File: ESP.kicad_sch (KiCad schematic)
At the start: 4 parts, among them SW1 RESET, U1 ESP32-C6-MINI-1/U

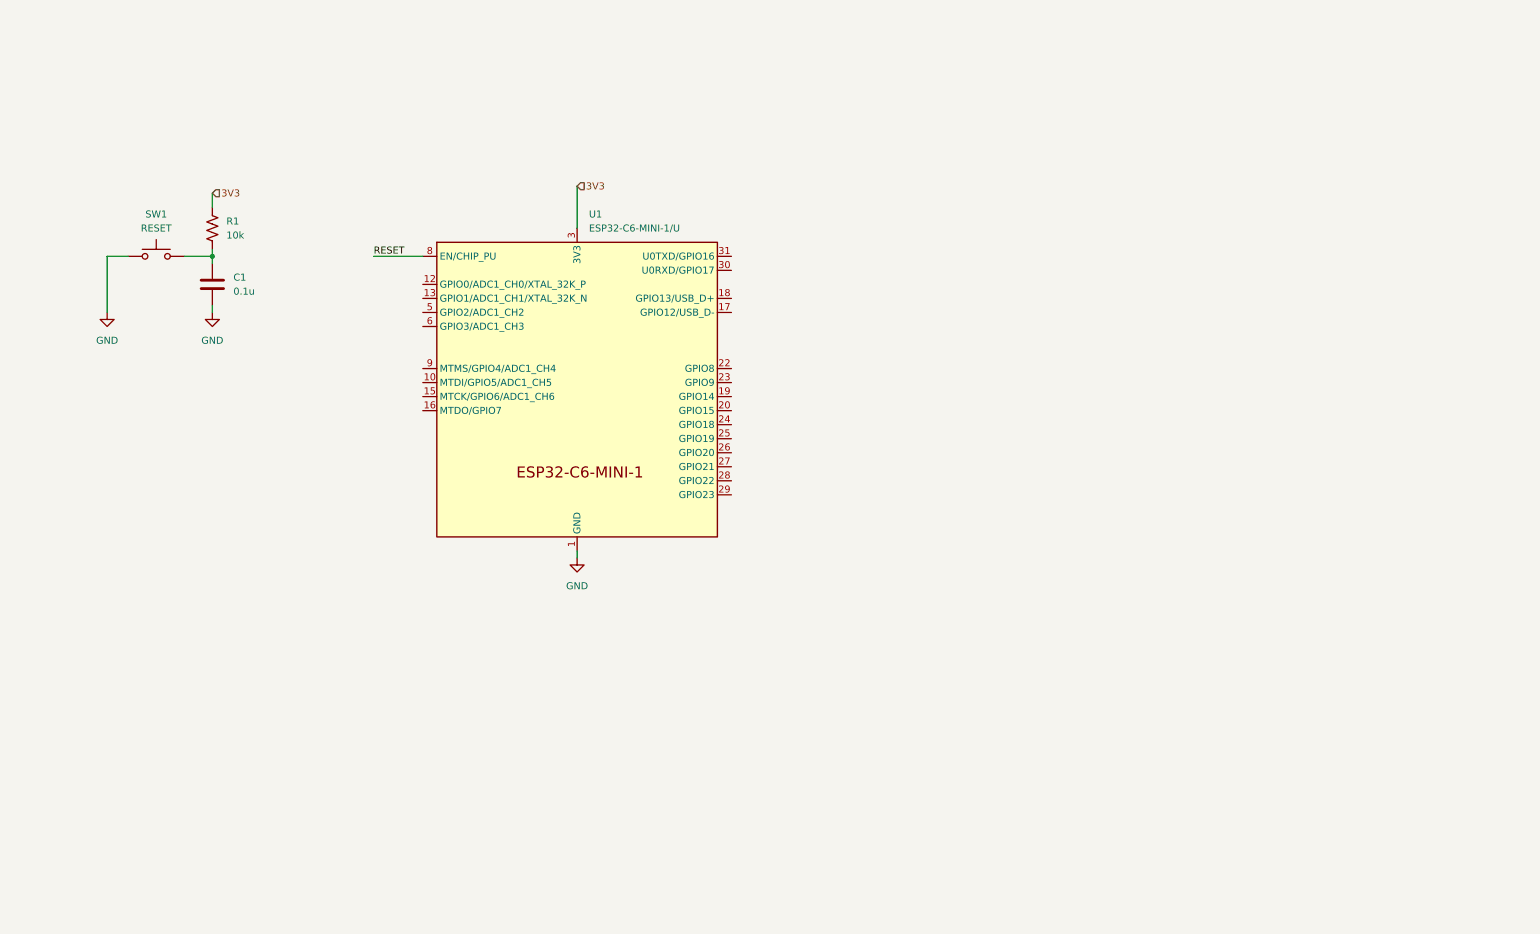
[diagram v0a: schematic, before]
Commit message: sch for review missing LSOM
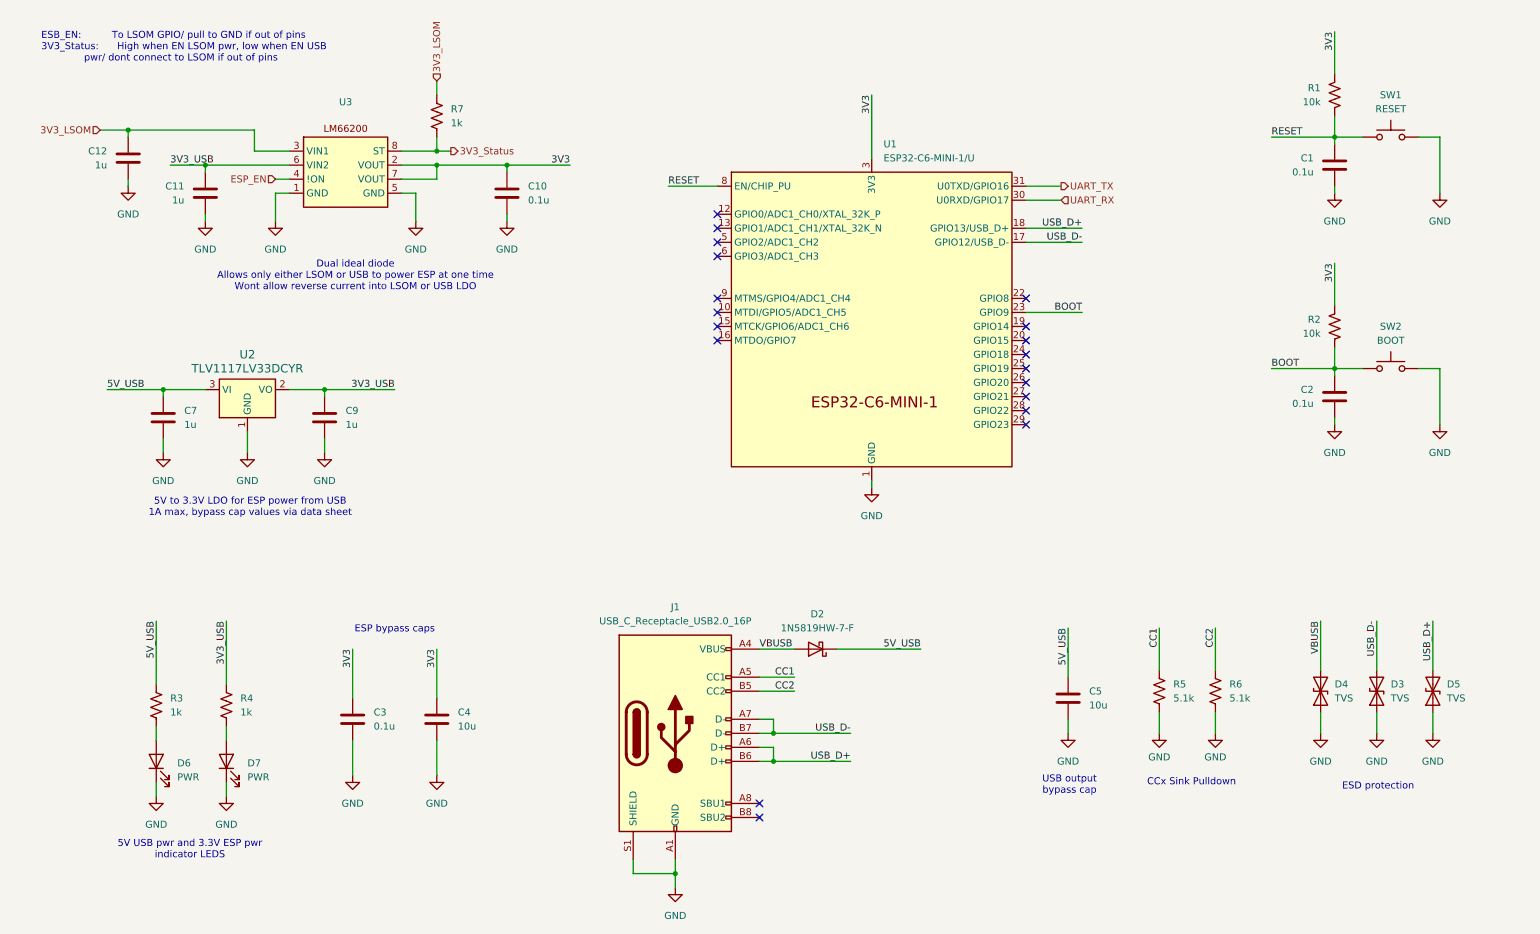
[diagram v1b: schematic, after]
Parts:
- added C10: 0.1u, Capacitor_SMD:C_0603_1608Metric, symbol Device:C
- added C11, C12, C7, C9: 1u, Capacitor_SMD:C_0603_1608Metric, symbol Device:C
- added C2, C3: 0.1u, symbol Device:C
- added C4: 10u, symbol Device:C
- added C5: 10u, Capacitor_SMD:C_0603_1608Metric, symbol Device:C
- added D2: 1N5819HW-7-F, Diode_SMD:D_SOD-123, symbol Device:D_Schottky
- added D3, D4, D5: TVS, Diode_SMD:D_0603_1608Metric, symbol Device:D_TVS
- added D6, D7: PWR, LED_SMD:LED_0603_1608Metric, symbol Device:LED
- added J1: USB_C_Receptacle_USB2.0_16P, Connector_USB:USB_C_Receptacle_GCT_USB4105-xx-A_16P_TopMnt_Horizontal, symbol Connector:USB_C_Receptacle_USB2.0_16P
- added R2: 10k, symbol Device:R_US
- added R3, R4, R7: 1k, symbol Device:R_US
- added R5, R6: 5.1k, symbol Device:R_US
- added SW2: BOOT, symbol Switch:SW_MEC_5G
- added U2: TLV1117LV33DCYR, Package_TO_SOT_SMD:SOT-223-3_TabPin2, symbol Regulator_Linear:AMS1117-3.3
- added U3: ~, symbol VCU:LM66200
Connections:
- net 3V3: now also C10.1, C3.1, C4.1, R2.1, U3.2 (VOUT), U3.7 (VOUT)
- net GND: now also C10.2, C11.2, C12.2, C2.2, C3.2, C4.2, C5.2, C7.2, C9.2, D3.1 (A1), D4.1 (A1), D5.1 (A1), D6.1 (K), D7.1 (K), J1.A1 (GND), J1.A12 (GND), J1.B1 (GND), J1.B12 (GND), J1.S1 (SHIELD), R5.2, R6.2, SW2.1 (A), SW2.2 (A), U2.1 (GND), U3.1 (GND), U3.5 (GND)
- net RESET: now also C1.1, R1.2, SW1.3 (B), SW1.4 (B)
- net USB_D-: now reaches U1.17 (GPIO12/USB_D-)
- net USB_D-: now also D3.2 (A2), J1.A7 (D-), J1.B7 (D-)
- net USB_D+: now reaches U1.18 (GPIO13/USB_D+)
- net USB_D+: now also D5.2 (A2), J1.A6 (D+), J1.B6 (D+)
- net BOOT: now reaches U1.23 (GPIO9)
- net BOOT: now also C2.1, R2.2, SW2.3 (B), SW2.4 (B)
- net UART_RX: now reaches U1.30 (U0RXD/GPIO17)
- net UART_TX: now reaches U1.31 (U0TXD/GPIO16)
- new net: D6.2 (A), R3.2
- new net: D7.2 (A), R4.2
- new net 3V3_LSOM: C12.1, R7.1, U3.3 (VIN1)
- new net 3V3_Status: R7.2, U3.8 (ST)
- new net 3V3_USB: C11.1, C9.1, R4.1, U2.2 (VO), U3.6 (VIN2)
- new net 5V_USB: C5.1, C7.1, D2.1 (K), R3.1, U2.3 (VI)
- new net CC1: J1.A5 (CC1), R5.1
- new net CC2: J1.B5 (CC2), R6.1
- new net ESP_EN: U3.4 (!ON)
- new net VBUSB: D2.2 (A), D4.2 (A2), J1.A4 (VBUS), J1.A9 (VBUS), J1.B4 (VBUS), J1.B9 (VBUS)
- no-connect marks 0 -> 19
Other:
- note added: "5V USB pwr and 3.3V ESP pwr indicator LEDS"
- note added: "5V to 3.3V LDO for ESP power from USB 1A max, bypass cap values via data sheet"
- note added: "CCx Sink Pulldown"
- note added: "Dual ideal diode Allows only either LSOM or USB to power ESP at one time Wont allow reverse current into LSOM or USB LDO"
- note added: "ESB_EN: To LSOM GPIO/ pull to GND if out of pins 3V3_Status: High when EN LSOM pwr, low when EN USB pwr/ dont connect to LSOM if out of pins"
- note added: "ESD protection"
- note added: "ESP bypass caps"
- note added: "USB output bypass cap"
- moved on the sheet: C1, R1, SW1, U1

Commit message: review LSOM
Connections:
- net 3V3_Status: no longer names the net of R7.2, U3.8 (ST)
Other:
- note added: "3V3_Status"
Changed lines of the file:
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@@
+		)
+	)
+	(text "3V3_Status"
+		(exclude_from_sim no)
+		(at 95.504 40.132 0)
+		(effects
+			(font
+				(size 1.27 1.27)
+			)
 		)
 	)
@@
 	)
 	(junction
-		(at 90.17 40.64)
-		(diameter 0)
-		(color 0 0 0 0)
-	)
-	(junction
 		(at 252.73 38.1)
 		(diameter 0)
@@
 	(wire
 		(pts
-			(xy 90.17 40.64) (xy 92.71 40.64)
-		)
-		(stroke
-			(width 0)
-			(type default)
-		)
-	)
-	(wire
-		(pts
 			(xy 148.59 151.13) (xy 151.13 151.13)
 		)
@@
 		)
 	)
-	(hierarchical_label "3V3_Status"
-		(shape output)
-		(at 92.71 40.64 0)
-		(effects
-			(font
-				(size 1.27 1.27)
-			)
-			(justify left)
-		)
-	)

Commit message: review sch one last time
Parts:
- removed C1, C2: 0.1u, symbol Device:C
- removed R1, R2: 10k, symbol Device:R_US
- removed SW1: RESET, symbol Switch:SW_MEC_5G
- removed SW2: BOOT, symbol Switch:SW_MEC_5G
- added J14: UART_Breakout, symbol Connector_Generic:Conn_01x02
- added R8: 10k, symbol Device:R_US
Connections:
- net GND: now also R8.2
- net UART_RX: now also J14.2 (Pin_2)
- net UART_TX: now also J14.1 (Pin_1)
- net LED1: now reaches U1.19 (GPIO14)
- net LED2: now reaches U1.20 (GPIO15)
- net LED3: now reaches U1.24 (GPIO18)
- net LED4: now reaches U1.25 (GPIO19)
- net IO1: now reaches U1.26 (GPIO20)
- net IO2: now reaches U1.27 (GPIO21)
- net IO3: now reaches U1.28 (GPIO22)
- net IO4: now reaches U1.29 (GPIO23)
- net ESP_EN: no longer names the net of U3.4 (!ON)
- net ESP_EN: now also R8.1
- no-connect marks 19 -> 11
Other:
- added sheet Buttons_LEDs_IO (Buttond_LEDs_IO.kicad_sch)
- note removed: "3V3_Status"
- note removed: "ESB_EN: To LSOM GPIO/ pull to GND if out of pins 3V3_Status: High when EN LSOM pwr, low when EN USB pwr/ dont connect to LSOM if out of pins"
- moved on the sheet: C10, C11, C12, C3, C4, C5, D2, D3, D4, D5, D6, D7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

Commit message: added opto's to sense signals
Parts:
- C3, C4: footprint (none) -> Capacitor_SMD:C_0805_2012Metric
- R3, R4, R5, R6, R7, R8: footprint (none) -> Resistor_SMD:R_0805_2012Metric
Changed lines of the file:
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@@
 			)
 		)
-		(property "Footprint" ""
+		(property "Footprint" "Resistor_SMD:R_0805_2012Metric"
 			(at 58.166 51.054 90)
 			(effects
@@
 			)
 		)
-		(property "Footprint" ""
+		(property "Footprint" "Capacitor_SMD:C_0805_2012Metric"
 			(at 55.5752 151.13 0)
 			(effects
@@
 			)
 		)
-		(property "Footprint" ""
+		(property "Footprint" "Resistor_SMD:R_0805_2012Metric"
 			(at 25.146 141.224 90)
 			(effects
@@
 			)
 		)
-		(property "Footprint" ""
+		(property "Footprint" "Resistor_SMD:R_0805_2012Metric"
 			(at 37.846 141.224 90)
 			(effects
@@
 			)
 		)
-		(property "Footprint" ""
+		(property "Footprint" "Resistor_SMD:R_0805_2012Metric"
 			(at 94.996 34.544 90)
 			(effects
@@
 			)
 		)
-		(property "Footprint" ""
+		(property "Footprint" "Resistor_SMD:R_0805_2012Metric"
 			(at 215.646 139.954 90)
 			(effects
@@
 			)
 		)
-		(property "Footprint" ""
+		(property "Footprint" "Capacitor_SMD:C_0805_2012Metric"
 			(at 68.8848 151.13 0)
 			(effects
@@
 			)
 		)
-		(property "Footprint" ""
+		(property "Footprint" "Resistor_SMD:R_0805_2012Metric"
 			(at 225.806 139.954 90)
 			(effects

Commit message: layout start
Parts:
- J13: renamed from J14; footprint (none) -> Connector_PinHeader_2.54mm:PinHeader_1x02_P2.54mm_Vertical
- U2: renamed from U3; footprint (none) -> LM66200:SOTFL50P160X60-8N
- U3: renamed from U1; footprint PCM_Espressif:ESP32-C6-MINI-1 -> ESP32-C6-MINI-1:ESP32-C6-MINI-1
- renumbered C5 to C10, C12 to C3, C7 to C4, C11 to C5, C3 to C6, C9 to C7, C4 to C8, C10 to C9, D6 to D2, D7 to D3, D2 to D4, D4 to D5, D3 to D6, D5 to D7, J1 to J12, R4 to R10, R8 to R11, R7 to R12, R5 to R13, R6 to R14, R3 to R9, U2 to U1

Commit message: first revision
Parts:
- J12: footprint Connector_USB:USB_C_Receptacle_GCT_USB4105-xx-A_16P_TopMnt_Horizontal -> USBC:GCT_USB4215-03-A_REVA
- renumbered C10 to C11, D5 to D6, D6 to D7, D7 to D8
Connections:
- net GND: now also J12.S2 (SHIELD), J12.S3 (SHIELD), J12.S4 (SHIELD)
- net IO12: now reaches U3.10 (MTDI/GPIO5/ADC1_CH5)
- net IO5: now reaches U3.12 (GPIO0/ADC1_CH0/XTAL_32K_P)
- net IO6: now reaches U3.13 (GPIO1/ADC1_CH1/XTAL_32K_N)
- net IO7: now reaches U3.15 (MTCK/GPIO6/ADC1_CH6)
- net IO8: now reaches U3.16 (MTDO/GPIO7)
- net IO9: now reaches U3.5 (GPIO2/ADC1_CH2)
- net IO10: now reaches U3.6 (GPIO3/ADC1_CH3)
- net IO11: now reaches U3.9 (MTMS/GPIO4/ADC1_CH4)
- no-connect marks 11 -> 3
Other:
- sheet Buttons_LEDs_IO ports: added IO10, IO11, IO12, IO5, IO6, IO7, IO8, IO9; removed none

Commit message: fixed
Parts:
- renumbered C11 to C10, D6 to D5, D7 to D6, D8 to D7
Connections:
- net IO1: now also U3.29 (GPIO23); no longer U3.26 (GPIO20)
- net IO10: now also U3.9 (MTMS/GPIO4/ADC1_CH4); no longer U3.6 (GPIO3/ADC1_CH3)
- net IO11: now also U3.6 (GPIO3/ADC1_CH3); no longer U3.9 (MTMS/GPIO4/ADC1_CH4)
- net IO12: now also U3.5 (GPIO2/ADC1_CH2); no longer U3.10 (MTDI/GPIO5/ADC1_CH5)
- net IO2: now also U3.28 (GPIO22); no longer U3.27 (GPIO21)
- net IO3: now also U3.27 (GPIO21); no longer U3.28 (GPIO22)
- net IO4: now also U3.26 (GPIO20); no longer U3.29 (GPIO23)
- net IO5: now also U3.16 (MTDO/GPIO7); no longer U3.12 (GPIO0/ADC1_CH0/XTAL_32K_P)
- net IO6: now also U3.15 (MTCK/GPIO6/ADC1_CH6); no longer U3.13 (GPIO1/ADC1_CH1/XTAL_32K_N)
- net IO7: now also U3.13 (GPIO1/ADC1_CH1/XTAL_32K_N); no longer U3.15 (MTCK/GPIO6/ADC1_CH6)
- net IO8: now also U3.12 (GPIO0/ADC1_CH0/XTAL_32K_P); no longer U3.16 (MTDO/GPIO7)
- net IO9: now also U3.10 (MTDI/GPIO5/ADC1_CH5); no longer U3.5 (GPIO2/ADC1_CH2)
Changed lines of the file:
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@@
 		)
 	)
-	(label "IO12"
+	(label "IO9"
 		(at 137.16 66.04 0)
 		(effects
@@
 		)
 	)
-	(label "IO7"
+	(label "IO6"
 		(at 137.16 68.58 0)
 		(effects
@@
 		)
 	)
-	(label "IO1"
+	(label "IO4"
 		(at 213.36 78.74 180)
 		(effects
@@
 		)
 	)
-	(label "IO9"
+	(label "IO12"
 		(at 137.16 53.34 0)
 		(effects
@@
 		)
 	)
-	(label "IO11"
+	(label "IO10"
 		(at 137.16 63.5 0)
 		(effects
@@
 		)
 	)
-	(label "IO3"
+	(label "IO2"
 		(at 213.36 83.82 180)
 		(effects
@@
 		)
 	)
-	(label "IO6"
+	(label "IO7"
 		(at 137.16 50.8 0)
 		(effects
@@
 		)
 	)
-	(label "IO5"
+	(label "IO8"
 		(at 137.16 48.26 0)
 		(effects
@@
 		)
 	)
-	(label "IO4"
+	(label "IO1"
 		(at 213.36 86.36 180)
 		(effects
@@
 		)
 	)
-	(label "IO8"
+	(label "IO5"
 		(at 137.16 71.12 0)
 		(effects
@@
 		)
 	)
-	(label "IO10"
+	(label "IO11"
 		(at 137.16 55.88 0)
 		(effects
@@
 		)
 	)
-	(label "IO2"
+	(label "IO3"
 		(at 213.36 81.28 180)
 		(effects
@@
 		(on_board yes)
 		(dnp no)
-		(property "Reference" "#PWR036"
+		(property "Reference" "#PWR034"
 			(at 214.63 153.67 0)
 			(effects
@@
 			(project "VehicleControlUnit"
 				(path "/795c8e51-3ded-4d21-b864-aaff31c5def7/6282503b-e4ab-454b-a074-f701a067f39b"
-					(reference "#PWR036")
+					(reference "#PWR034")
 					(unit 1)
 				)
@@
 		(dnp no)
 		(fields_autoplaced yes)
-		(property "Reference" "#PWR034"
+		(property "Reference" "#PWR032"
 			(at 175.26 104.14 0)
 			(effects
@@
 			(project ""
 				(path "/795c8e51-3ded-4d21-b864-aaff31c5def7/6282503b-e4ab-454b-a074-f701a067f39b"
-					(reference "#PWR034")
+					(reference "#PWR032")
 					(unit 1)
 				)
@@
 		(dnp no)
 		(fields_autoplaced yes)
-		(property "Reference" "D7"
+		(property "Reference" "D6"
 			(at 256.54 138.4299 90)
 			(effects
@@
 			(project "VehicleControlUnit"
 				(path "/795c8e51-3ded-4d21-b864-aaff31c5def7/6282503b-e4ab-454b-a074-f701a067f39b"
-					(reference "D7")
+					(reference "D6")
 					(unit 1)
 				)
@@
 		(dnp no)
 		(fields_autoplaced yes)
-		(property "Reference" "#PWR035"
+		(property "Reference" "#PWR033"
 			(at 198.12 153.67 0)
 			(effects
@@
 			(project "VehicleControlUnit"
 				(path "/795c8e51-3ded-4d21-b864-aaff31c5def7/6282503b-e4ab-454b-a074-f701a067f39b"
-					(reference "#PWR035")
+					(reference "#PWR033")
 					(unit 1)
 				)
@@
 		(dnp no)
 		(fields_autoplaced yes)
-		(property "Reference" "#PWR039"
+		(property "Reference" "#PWR037"
 			(at 254 153.67 0)
 			(effects
@@
 			(project "VehicleControlUnit"
 				(path "/795c8e51-3ded-4d21-b864-aaff31c5def7/6282503b-e4ab-454b-a074-f701a067f39b"
-					(reference "#PWR039")
+					(reference "#PWR037")
 					(unit 1)
 				)
@@
 		(dnp no)
 		(fields_autoplaced yes)
-		(property "Reference" "#PWR038"
+		(property "Reference" "#PWR036"
 			(at 243.84 153.67 0)
 			(effects
@@
 			(project "VehicleControlUnit"
 				(path "/795c8e51-3ded-4d21-b864-aaff31c5def7/6282503b-e4ab-454b-a074-f701a067f39b"
-					(reference "#PWR038")
+					(reference "#PWR036")
 					(unit 1)
 				)
@@
 		(dnp no)
 		(fields_autoplaced yes)
-		(property "Reference" "#PWR040"
+		(property "Reference" "#PWR038"
 			(at 264.16 153.67 0)
 			(effects
@@
 			(project "VehicleControlUnit"
 				(path "/795c8e51-3ded-4d21-b864-aaff31c5def7/6282503b-e4ab-454b-a074-f701a067f39b"
-					(reference "#PWR040")
+					(reference "#PWR038")
 					(unit 1)
 				)
@@
 		(on_board yes)
 		(dnp no)
-		(property "Reference" "#PWR037"
+		(property "Reference" "#PWR035"
 			(at 224.79 153.67 0)
 			(effects
@@
 			(project "VehicleControlUnit"
 				(path "/795c8e51-3ded-4d21-b864-aaff31c5def7/6282503b-e4ab-454b-a074-f701a067f39b"
-					(reference "#PWR037")
+					(reference "#PWR035")
 					(unit 1)
 				)
@@
 		(dnp no)
 		(fields_autoplaced yes)
-		(property "Reference" "C11"
+		(property "Reference" "C10"
 			(at 201.93 139.6999 0)
 			(effects
@@
 			(project "VehicleControlUnit"
 				(path "/795c8e51-3ded-4d21-b864-aaff31c5def7/6282503b-e4ab-454b-a074-f701a067f39b"
-					(reference "C11")
+					(reference "C10")
 					(unit 1)
 				)
@@
 		(dnp no)
 		(fields_autoplaced yes)
-		(property "Reference" "D8"
+		(property "Reference" "D7"
 			(at 266.7 138.4299 90)
 			(effects
@@
 			(project "VehicleControlUnit"
 				(path "/795c8e51-3ded-4d21-b864-aaff31c5def7/6282503b-e4ab-454b-a074-f701a067f39b"
-					(reference "D8")
+					(reference "D7")
 					(unit 1)
 				)
@@
 		(dnp no)
 		(fields_autoplaced yes)
-		(property "Reference" "D6"
+		(property "Reference" "D5"
 			(at 246.38 138.4299 90)
 			(effects
@@
 			(project "VehicleControlUnit"
 				(path "/795c8e51-3ded-4d21-b864-aaff31c5def7/6282503b-e4ab-454b-a074-f701a067f39b"
-					(reference "D6")
+					(reference "D5")
 					(unit 1)
 				)
